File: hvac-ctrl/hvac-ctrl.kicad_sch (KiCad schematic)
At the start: 18 parts, among them J1 Screw_Terminal_01x03, J2 Screw_Terminal_01x02, J3 Screw_Terminal_01x03, J4 Screw_Terminal_01x02, J5 EMR_x4, J6 EMR_x2, J7 SSR_x2, J8 Raspberry_Pi_1, U1 Module_LM2596_ADJ, U2 Module_LM2596_ADJ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

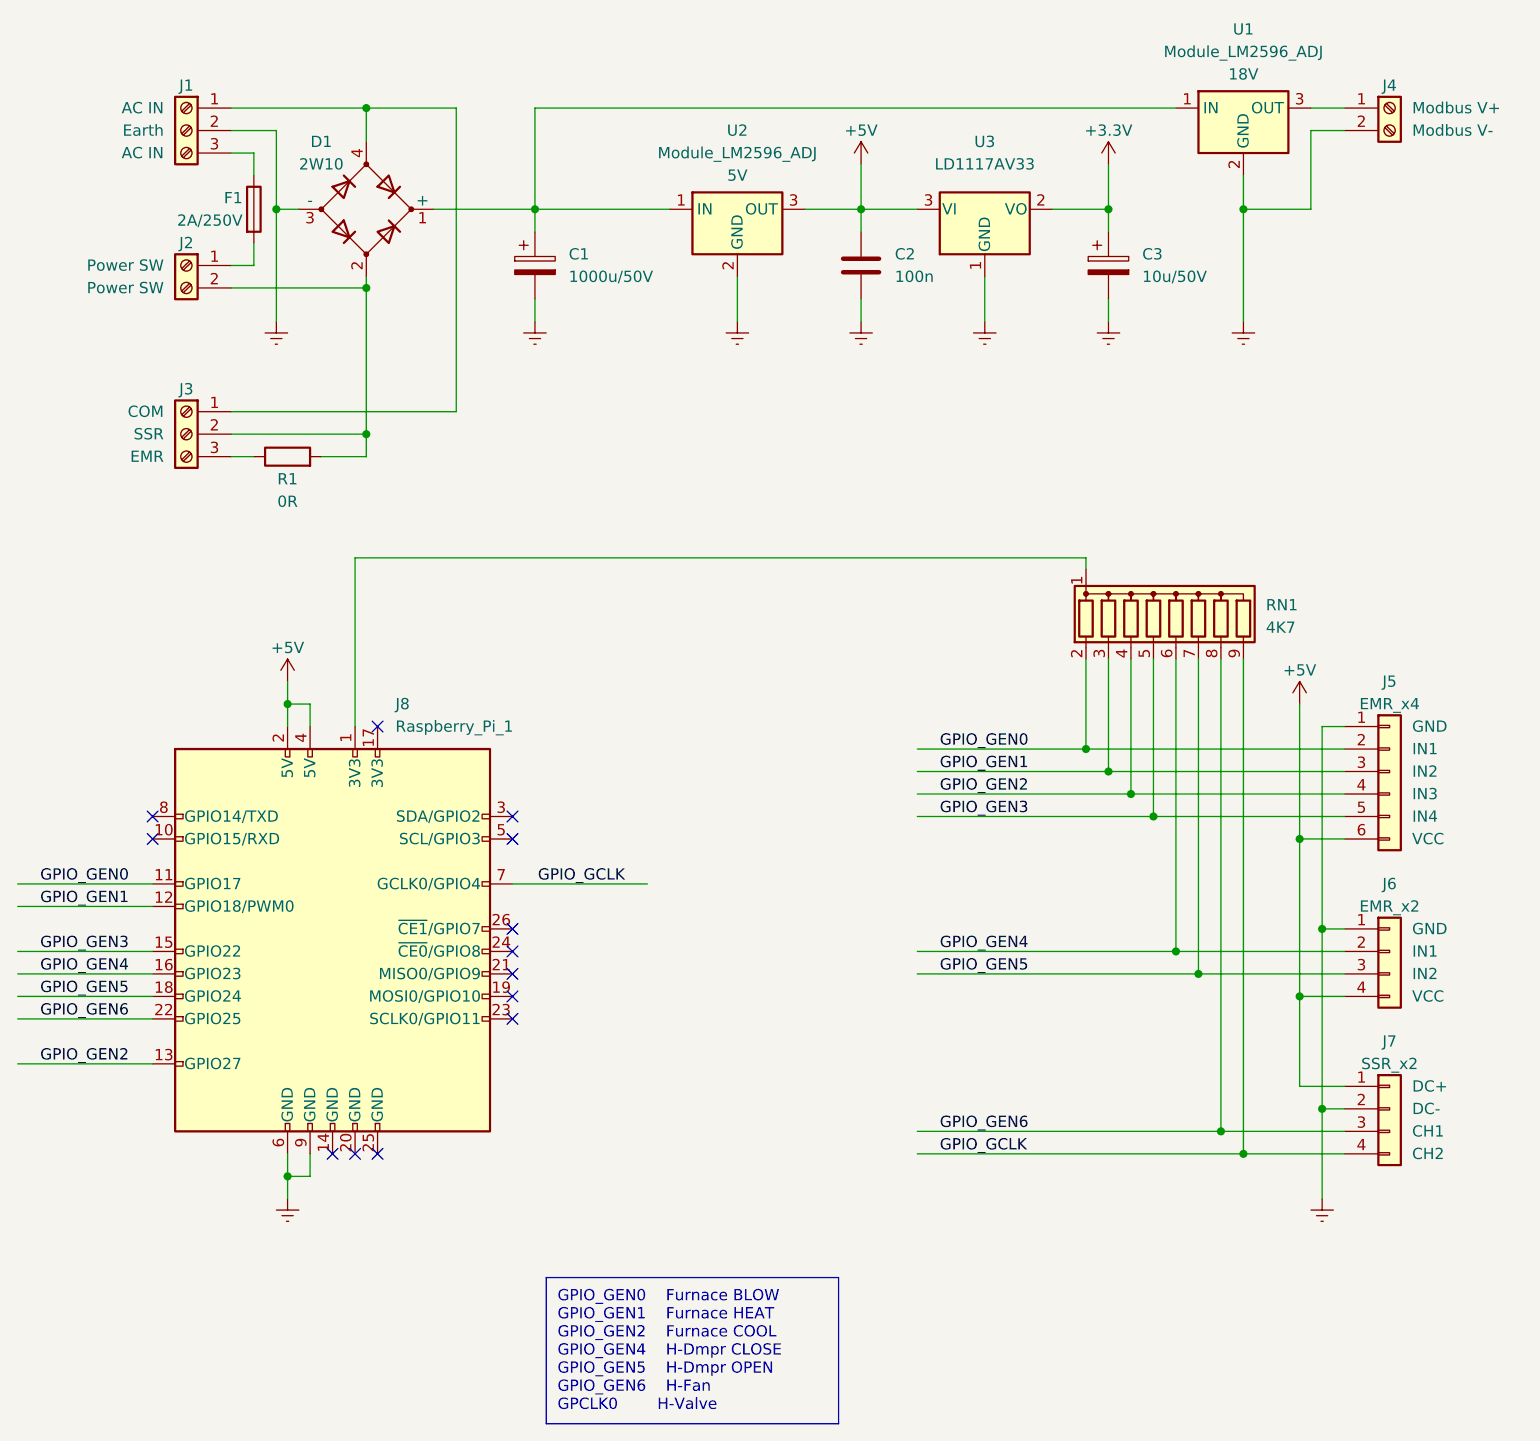
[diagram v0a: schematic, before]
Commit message: Add PCF8575 IO expander and ERV control block
HW version 1.3 (Dec 30, 2022)
- move GPIO control from Raspberry Pi to PCF8575 IO expander module
- add ERV control block based on LTV-847 optocoupler
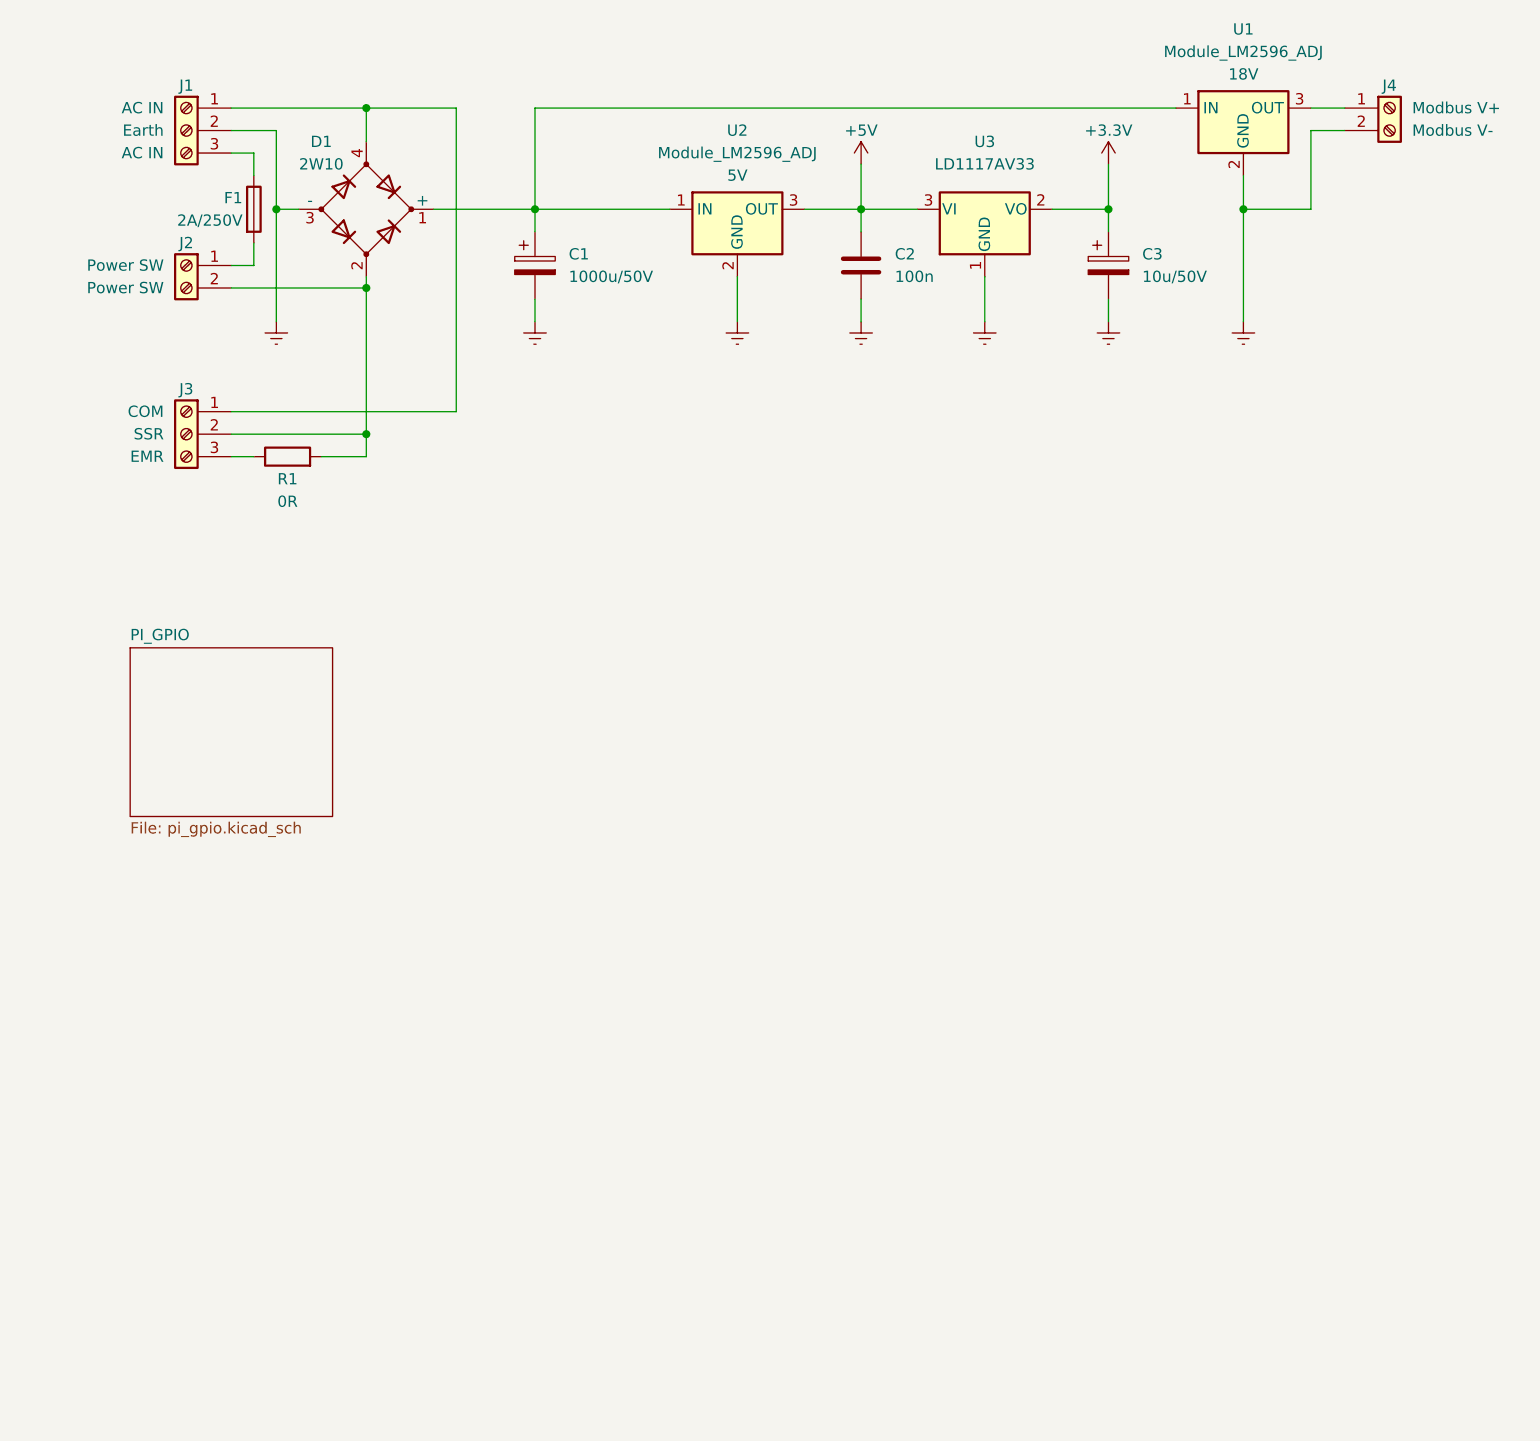
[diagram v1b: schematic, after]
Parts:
- removed J5: EMR_x4, Connector_PinHeader_2.54mm:PinHeader_1x06_P2.54mm_Horizontal, symbol Connector_Generic:Conn_01x06
- removed J6: EMR_x2, symbol Connector_Generic:Conn_01x04
- removed J7: SSR_x2, symbol Connector_Generic:Conn_01x04
- removed J8: Raspberry_Pi_1, symbol _Connector:Raspberry_Pi_1
- removed RN1: 4K7, Resistor_THT:R_Array_SIP9, symbol Device:R_Network08
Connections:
- no-connect marks 13 -> 0
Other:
- added sheet PI_GPIO (pi_gpio.kicad_sch)
- note removed: "GPIO_GEN0 Furnace BLOW GPIO_GEN1 Furnace HEAT GPIO_GEN2 Furnace COOL GPIO_GEN4 H-Dmpr CLOSE GPIO_GEN5 H-Dmpr OPEN GPIO_GEN6 H-Fan GPCLK0 H-Valve"
